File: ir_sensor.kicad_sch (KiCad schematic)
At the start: 9 parts, among them U7 LM358

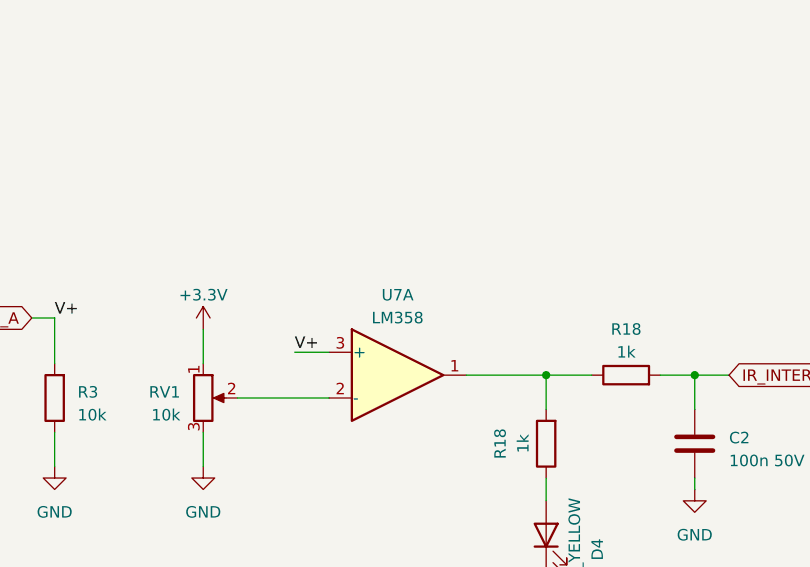
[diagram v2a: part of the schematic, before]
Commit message: Add hysteresis to IR sensor. Update README file.
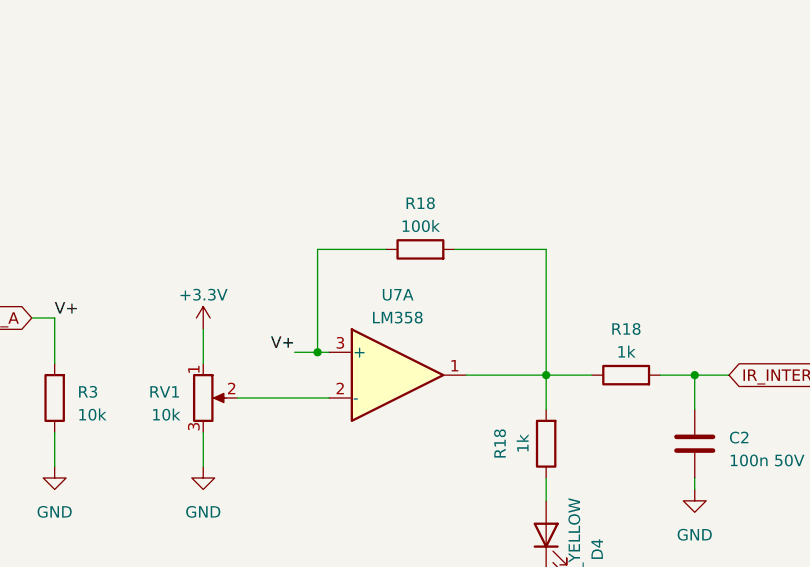
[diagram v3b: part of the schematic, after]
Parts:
- added R18: 100k, Resistor_SMD:R_0402_1005Metric, symbol Device:R
- C2: footprint Capacitor_SMD:C_01005_0402Metric -> Capacitor_SMD:C_0402_1005Metric
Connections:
- net IR_SENSE_A: now also R18.1
- net at R18.1, R18.2, U7.1: now also R18.2
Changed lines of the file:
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@@
   (junction (at 54.61 30.48) (diameter 0) (color 0 0 0 0)
   )
-  (wire (pts (xy 129.54 87.63) (xy 133.35 87.63))
+  (junction (at 132.08 87.63) (diameter 0) (color 0 0 0 0)
+  )
+  (wire (pts (xy 129.54 87.63) (xy 132.08 87.63))
     (stroke (width 0) (type default))
   )
@@
     (stroke (width 0) (type default))
   )
+  (wire (pts (xy 132.08 87.63) (xy 133.35 87.63))
+    (stroke (width 0) (type default))
+  )
   (wire (pts (xy 173.99 102.87) (xy 173.99 101.6))
     (stroke (width 0) (type default))
@@
     (stroke (width 0) (type default))
   )
+  (wire (pts (xy 157.48 76.2) (xy 157.48 90.17))
+    (stroke (width 0) (type default))
+  )
   (wire (pts (xy 54.61 41.91) (xy 54.61 40.64))
     (stroke (width 0) (type default))
   )
+  (wire (pts (xy 132.08 76.2) (xy 132.08 87.63))
+    (stroke (width 0) (type default))
+  )
   (wire (pts (xy 123.19 92.71) (xy 133.35 92.71))
     (stroke (width 0) (type default))
@@
     (stroke (width 0) (type default))
   )
+  (wire (pts (xy 147.32 76.2) (xy 157.48 76.2))
+    (stroke (width 0) (type default))
+  )
   (wire (pts (xy 82.55 83.82) (xy 82.55 88.9))
     (stroke (width 0) (type default))
@@
   )
   (wire (pts (xy 102.87 96.52) (xy 102.87 100.33))
+    (stroke (width 0) (type default))
+  )
+  (wire (pts (xy 139.7 76.2) (xy 132.08 76.2))
     (stroke (width 0) (type default))
   )
@@
     (effects (font (size 2.5654 2.5654) (thickness 0.5131) bold) (justify right bottom))
   )
-  (label "V+" (at 129.54 87.63 0) (fields_autoplaced)
-    (effects (font (size 1.27 1.27)) (justify left bottom))
+  (label "V+" (at 129.54 87.63 180) (fields_autoplaced)
+    (effects (font (size 1.27 1.27)) (justify right bottom))
   )
   (label "V+" (at 102.87 83.82 0) (fields_autoplaced)
@@
       (effects (font (size 1.27 1.27)) (justify left))
     )
-    (property "Footprint" "Capacitor_SMD:C_01005_0402Metric" (at 174.9552 101.6 0)
+    (property "Footprint" "Capacitor_SMD:C_0402_1005Metric" (at 174.9552 101.6 0)
       (effects (font (size 1.27 1.27)) hide)
     )
@@
       (effects (font (size 1.27 1.27)) (justify left))
     )
-    (property "Footprint" "Capacitor_SMD:C_01005_0402Metric" (at 55.5752 40.64 0)
+    (property "Footprint" "Capacitor_SMD:C_0402_1005Metric" (at 55.5752 40.64 0)
       (effects (font (size 1.27 1.27)) hide)
     )
@@
         )
       )
+    )
+  )
+  (symbol (lib_id "Device:R") (at 143.51 76.2 90) (unit 1)
+    (in_bom yes) (on_board yes) (dnp no)
+    (property "Reference" "R18" (at 143.51 71.12 90)
+      (effects (font (size 1.27 1.27)))
+    )
+    (property "Value" "100k" (at 143.51 73.66 90)
+      (effects (font (size 1.27 1.27)))
+    )
+    (property "Footprint" "Resistor_SMD:R_0402_1005Metric" (at 143.51 77.978 90)
+      (effects (font (size 1.27 1.27)) hide)
+    )
+    (property "Datasheet" "~" (at 143.51 76.2 0)
+      (effects (font (size 1.27 1.27)) hide)
+    )
+    (property "LCSC" "C25741" (at 143.51 76.2 0)
+      (effects (font (size 1.27 1.27)) hide)
+    )
+    (pin "1")
+    (pin "2")
+    (instances
+      (project "DPB-PCB"
+        (path "/0a09ce58-c923-4e96-b56b-0b86aca559ed/092167cc-e573-4c90-9993-424a50e31da7"
+          (reference "R18") (unit 1)
+        )
+        (path "/0a09ce58-c923-4e96-b56b-0b86aca559ed/37faa5be-535b-4559-acf1-df3dbabb2c7b"
+          (reference "R10") (unit 1)
+        )
+        (path "/0a09ce58-c923-4e96-b56b-0b86aca559ed/13b734dc-9ebc-48a5-b407-7a67b1b686cd"
+          (reference "R43") (unit 1)
+        )
+      )
